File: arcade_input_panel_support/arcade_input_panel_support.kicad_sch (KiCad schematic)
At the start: 14 parts, among them J1 Conn_01x15, J10 Conn_01x02, J11 Conn_01x02, J12 Conn_01x02, J13 Conn_01x02, J14 Conn_01x02, J2 Conn_01x14, J3 Conn_01x15, J4 Conn_01x15, J5 Conn_01x05, J6 Conn_01x02, J7 Conn_01x02, J8 Conn_01x02, J9 Conn_01x02

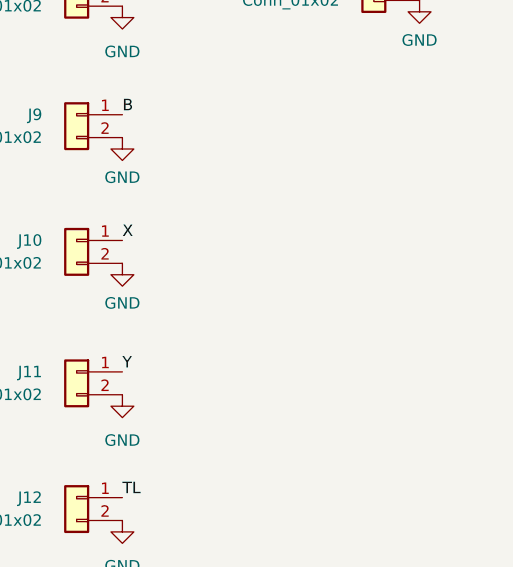
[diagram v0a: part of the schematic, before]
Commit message: 커넥터 추가
Signed-off-by: Ju, Gyeong-min <jcmh74@gmail.com>
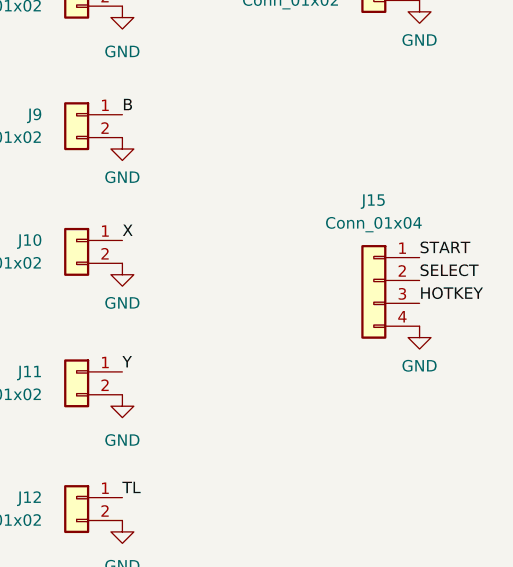
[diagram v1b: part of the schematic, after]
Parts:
- added J15: Conn_01x04, Connector_PinHeader_2.54mm:PinHeader_1x04_P2.54mm_Vertical, symbol Connector_Generic:Conn_01x04
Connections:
- net GND: now also J15.4 (Pin_4)
- net HOTKEY: now also J15.3 (Pin_3)
- net SELECT: now also J15.2 (Pin_2)
- net START: now also J15.1 (Pin_1)
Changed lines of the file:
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@@
     (title "Input Panel Support")
     (date "2023-12-08")
-    (rev "1")
+    (rev "2")
     (company "Amos Home")
   )
@@
     (effects (font (size 1.27 1.27)) (justify left bottom))
   )
+  (label "START" (at 220.345 83.82 0) (fields_autoplaced)
+    (effects (font (size 1.27 1.27)) (justify left bottom))
+  )
   (label "B" (at 74.93 121.285 0) (fields_autoplaced)
     (effects (font (size 1.27 1.27)) (justify left bottom))
@@
     (effects (font (size 1.27 1.27)) (justify left bottom))
   )
+  (label "SELECT" (at 220.345 86.36 0) (fields_autoplaced)
+    (effects (font (size 1.27 1.27)) (justify left bottom))
+  )
   (label "A" (at 74.93 118.745 0) (fields_autoplaced)
     (effects (font (size 1.27 1.27)) (justify left bottom))
@@
     (effects (font (size 1.27 1.27)) (justify left bottom))
   )
+  (label "HOTKEY" (at 220.345 88.9 0) (fields_autoplaced)
+    (effects (font (size 1.27 1.27)) (justify left bottom))
+  )
   (label "RIGHT" (at 106.045 61.595 0) (fields_autoplaced)
     (effects (font (size 1.27 1.27)) (justify left bottom))
@@
         (path "/e63e39d7-6ac0-4ffd-8aa3-1841a4541b55"
           (reference "#PWR07") (unit 1)
+        )
+      )
+    )
+  )
+  (symbol (lib_id "power:GND") (at 220.345 91.44 0) (unit 1)
+    (in_bom yes) (on_board yes) (dnp no) (fields_autoplaced)
+    (property "Reference" "#PWR019" (at 220.345 97.79 0)
+      (effects (font (size 1.27 1.27)) hide)
+    )
+    (property "Value" "GND" (at 220.345 95.885 0)
+      (effects (font (size 1.27 1.27)))
+    )
+    (property "Footprint" "" (at 220.345 91.44 0)
+      (effects (font (size 1.27 1.27)) hide)
+    )
+    (property "Datasheet" "" (at 220.345 91.44 0)
+      (effects (font (size 1.27 1.27)) hide)
+    )
+    (pin "1")
+    (instances
+      (project "arcade_input_panel_support"
+        (path "/e63e39d7-6ac0-4ffd-8aa3-1841a4541b55"
+          (reference "#PWR019") (unit 1)
         )
       )
@@
         )
       )
+    )
+  )
+  (symbol (lib_id "Connector_Generic:Conn_01x04") (at 215.265 86.36 0) (mirror y) (unit 1)
+    (in_bom yes) (on_board yes) (dnp no) (fields_autoplaced)
+    (property "Reference" "J15" (at 215.265 77.47 0)
+      (effects (font (size 1.27 1.27)))
+    )
+    (property "Value" "Conn_01x04" (at 215.265 80.01 0)
+      (effects (font (size 1.27 1.27)))
+    )
+    (property "Footprint" "Connector_PinHeader_2.54mm:PinHeader_1x04_P2.54mm_Vertical" (at 215.265 86.36 0)
+      (effects (font (size 1.27 1.27)) hide)
+    )
+    (property "Datasheet" "~" (at 215.265 86.36 0)
+      (effects (font (size 1.27 1.27)) hide)
+    )
+    (pin "2")
+    (pin "3")
+    (pin "1")
+    (pin "4")
+    (instances
+      (project "arcade_input_panel_support"
+        (path "/e63e39d7-6ac0-4ffd-8aa3-1841a4541b55"
+          (reference "J15") (unit 1)
+        )
+      )

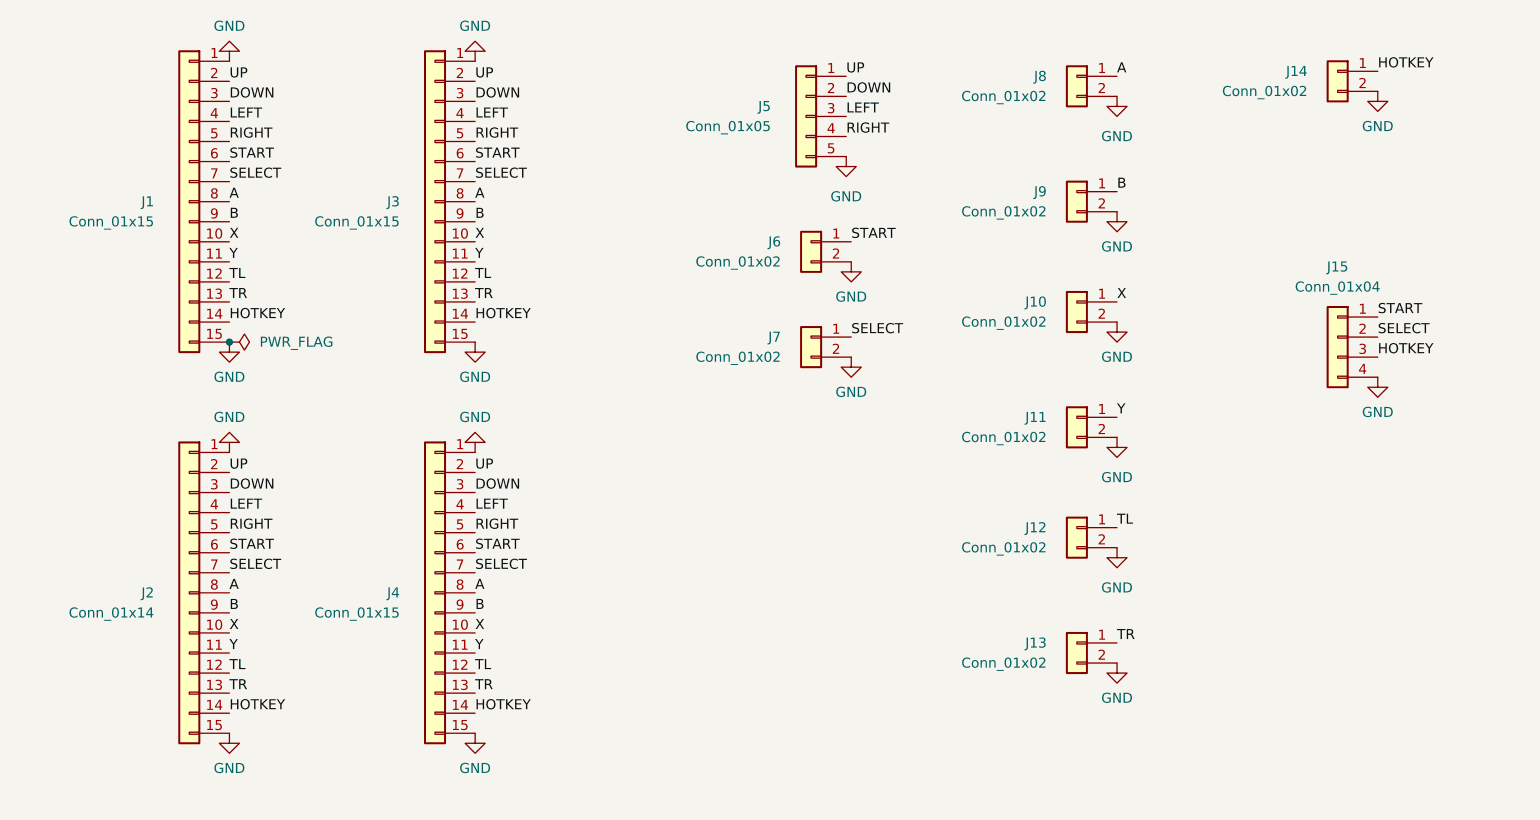
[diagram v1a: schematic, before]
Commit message: 입력 패널 버튼 서포터 rev 2
Signed-off-by: Ju, Gyeong-min <jcmh74@gmail.com>
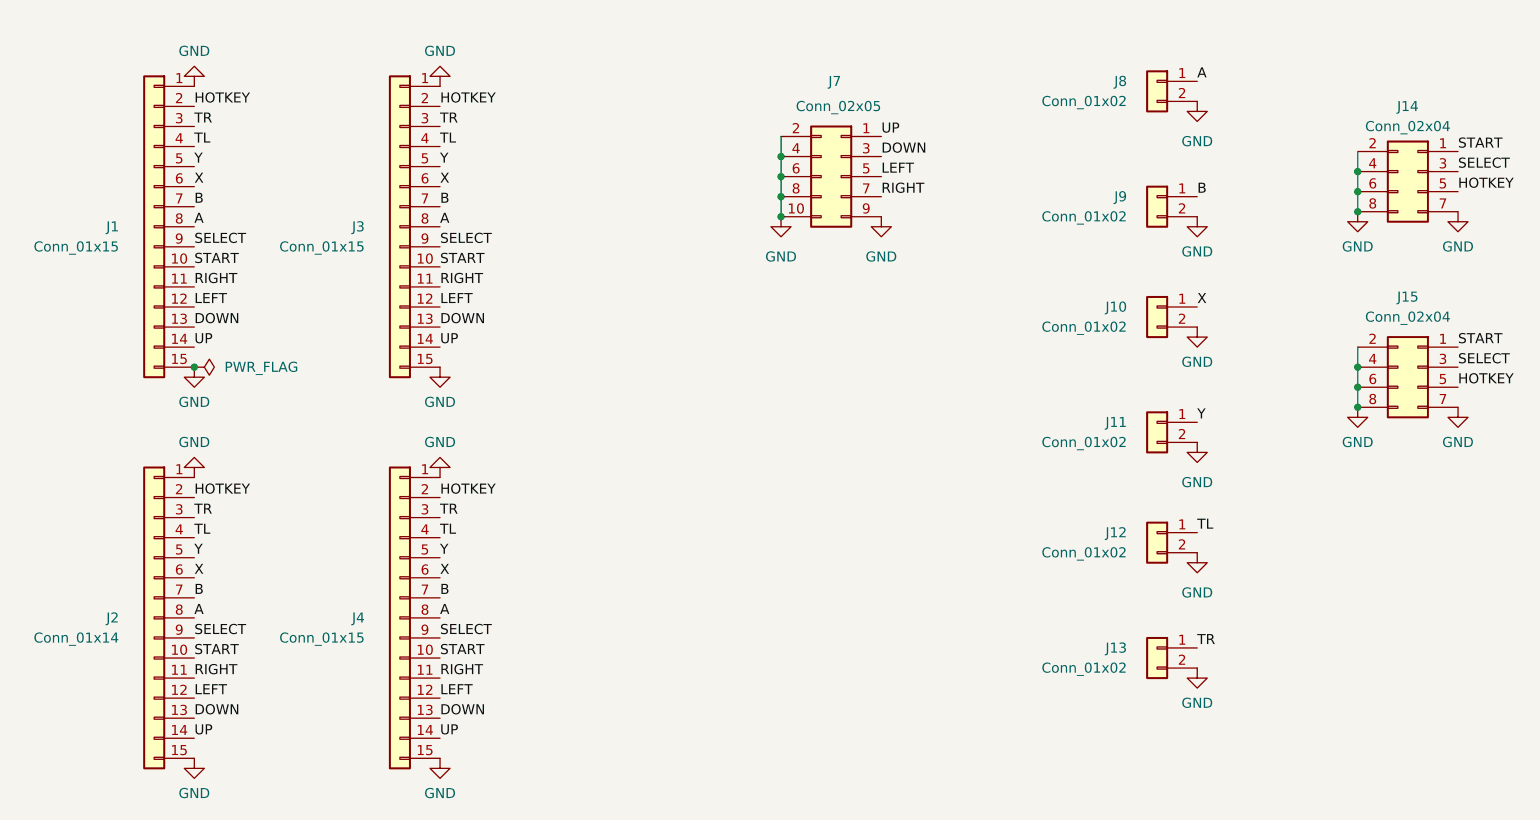
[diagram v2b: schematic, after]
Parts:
- removed J14, J6, J7: Conn_01x02, Connector_PinHeader_2.54mm:PinHeader_1x02_P2.54mm_Vertical, symbol Connector_Generic:Conn_01x02
- added J15: Conn_02x04, Connector_PinHeader_2.54mm:PinHeader_2x04_P2.54mm_Vertical, symbol Connector_Generic:Conn_02x04_Odd_Even
- J14: renamed from J15; value Conn_01x04 -> Conn_02x04; footprint Connector_PinHeader_2.54mm:PinHeader_1x04_P2.54mm_Vertical -> Connector_PinHeader_2.54mm:PinHeader_2x04_P2.54mm_Vertical; symbol Connector_Generic:Conn_01x04 -> Connector_Generic:Conn_02x04_Odd_Even
- J7: renamed from J5; value Conn_01x05 -> Conn_02x05; footprint Connector_PinHeader_2.54mm:PinHeader_1x05_P2.54mm_Vertical -> Connector_PinHeader_2.54mm:PinHeader_2x05_P2.54mm_Vertical; symbol Connector_Generic:Conn_01x05 -> Connector_Generic:Conn_02x05_Odd_Even
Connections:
- net B: now also J1.7 (Pin_7), J2.7 (Pin_7), J3.7 (Pin_7), J4.7 (Pin_7); no longer J1.9 (Pin_9), J2.9 (Pin_9), J3.9 (Pin_9), J4.9 (Pin_9)
- net DOWN: now also J1.13 (Pin_13), J2.13 (Pin_13), J3.13 (Pin_13), J4.13 (Pin_13), J7.3 (Pin_3); no longer J1.3 (Pin_3), J2.3 (Pin_3), J3.3 (Pin_3), J4.3 (Pin_3), J7.2 (Pin_2)
- net GND: now also J14.2 (Pin_2), J14.6 (Pin_6), J14.7 (Pin_7), J14.8 (Pin_8), J7.10 (Pin_10), J7.2 (Pin_2), J7.4 (Pin_4), J7.6 (Pin_6), J7.8 (Pin_8), J7.9 (Pin_9), J15.2 (Pin_2), J15.4 (Pin_4), J15.6 (Pin_6), J15.7 (Pin_7), J15.8 (Pin_8); no longer J7.5 (Pin_5)
- net HOTKEY: now also J1.2 (Pin_2), J14.5 (Pin_5), J2.2 (Pin_2), J3.2 (Pin_2), J4.2 (Pin_2), J15.5 (Pin_5); no longer J1.14 (Pin_14), J14.3 (Pin_3), J2.14 (Pin_14), J3.14 (Pin_14), J4.14 (Pin_14)
- net LEFT: now also J1.12 (Pin_12), J2.12 (Pin_12), J3.12 (Pin_12), J4.12 (Pin_12), J7.5 (Pin_5); no longer J1.4 (Pin_4), J2.4 (Pin_4), J3.4 (Pin_4), J4.4 (Pin_4), J7.3 (Pin_3)
- net RIGHT: now also J1.11 (Pin_11), J2.11 (Pin_11), J3.11 (Pin_11), J4.11 (Pin_11), J7.7 (Pin_7); no longer J1.5 (Pin_5), J2.5 (Pin_5), J3.5 (Pin_5), J4.5 (Pin_5), J7.4 (Pin_4)
- net SELECT: now also J1.9 (Pin_9), J14.3 (Pin_3), J2.9 (Pin_9), J3.9 (Pin_9), J4.9 (Pin_9), J15.3 (Pin_3); no longer J1.7 (Pin_7), J14.2 (Pin_2), J2.7 (Pin_7), J3.7 (Pin_7), J4.7 (Pin_7)
- net START: now also J1.10 (Pin_10), J2.10 (Pin_10), J3.10 (Pin_10), J4.10 (Pin_10), J15.1 (Pin_1); no longer J1.6 (Pin_6), J2.6 (Pin_6), J3.6 (Pin_6), J4.6 (Pin_6)
- net TL: now also J1.4 (Pin_4), J2.4 (Pin_4), J3.4 (Pin_4), J4.4 (Pin_4); no longer J1.12 (Pin_12), J2.12 (Pin_12), J3.12 (Pin_12), J4.12 (Pin_12)
- net TR: now also J1.3 (Pin_3), J2.3 (Pin_3), J3.3 (Pin_3), J4.3 (Pin_3); no longer J1.13 (Pin_13), J2.13 (Pin_13), J3.13 (Pin_13), J4.13 (Pin_13)
- net UP: now also J1.14 (Pin_14), J2.14 (Pin_14), J3.14 (Pin_14), J4.14 (Pin_14); no longer J1.2 (Pin_2), J2.2 (Pin_2), J3.2 (Pin_2), J4.2 (Pin_2)
- net X: now also J1.6 (Pin_6), J2.6 (Pin_6), J3.6 (Pin_6), J4.6 (Pin_6); no longer J1.10 (Pin_10), J2.10 (Pin_10), J3.10 (Pin_10), J4.10 (Pin_10)
- net Y: now also J1.5 (Pin_5), J2.5 (Pin_5), J3.5 (Pin_5), J4.5 (Pin_5); no longer J1.11 (Pin_11), J2.11 (Pin_11), J3.11 (Pin_11), J4.11 (Pin_11)
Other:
- moved on the sheet: J1, J10, J11, J12, J13, J2, J3, J4, J8, J9
